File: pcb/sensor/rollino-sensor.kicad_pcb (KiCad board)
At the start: 2 copper layers, 27.5 x 23.2 mm, 14 parts, among them J1 FH12-6S-0.5SH, U1 PMW3610DM-SUDU, U2 TPS7A0518PDBVR

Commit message: Route both PCBs, copper logo, 3D renders of the boards
pcb/gen/route.py has Freerouting route every net (edge and logo keep-outs,
retrying strategies until nothing is left unconnected) and pours GND;
pcb/gen/render_pcbs.sh renders both boards in Blender from KiCad's VRML,
with generated models for the upside-down XIAO and the PMW3610 + lens. The
ROLLINO logo is now bare copper on the back of the band instead of
silkscreen cut by the XIAO's cutout. Connector mounting tabs go to GND;
mounting holes have symbols; the band is 0.5 mm wider for the connectors'
escape routes.

Co-Authored-By: Claude Opus 5.5 <noreply@anthropic.com>
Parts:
- moved U2 0.40 mm to (150.8, 92.1), turned to 180 degrees
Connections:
- net CN renamed /CN
- net CP renamed /CP
- net MOTION renamed /MOTION
- net NCS renamed /NCS
- net NRESET renamed /NRESET
- net SCLK renamed /SCLK
- net SDIO renamed /SDIO
- net VCP renamed /VCP
- net VCSEL+ renamed /VCSEL+
- net VCSEL- renamed /VCSEL-
- J1 pad MP: (no net) -> GND
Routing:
- net +3V3: track 0.00 -> 61.2 mm, vias 0 -> 1
- net GND: track 0.00 -> 59.9 mm, vias 0 -> 1
- net +1V8: track 0.00 -> 48.0 mm, vias 0 -> 1
- net /VCSEL+: track 0.00 -> 46.5 mm, vias 0 -> 1
- net /SDIO: track 0.00 -> 25.5 mm, vias 0 -> 1
- net /SCLK: track 0.00 -> 24.5 mm, vias 0 -> 1
- net /NCS: track 0.00 -> 19.1 mm, vias 0 -> 1
- net /MOTION: track 0.00 -> 13.1 mm, vias 0 -> 1
- net /VCP: track 0.00 -> 5.85 mm, vias 0 -> 1
- net /CP: track 0.00 -> 3.87 mm
- net /CN: track 0.00 -> 2.37 mm
- net /NRESET: track 0.00 -> 2.18 mm
- net /VCSEL-: track 0.00 -> 1.78 mm
- added copper zone on B.Cu, net GND
- added copper zone on F.Cu, net GND
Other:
- board text removed: "ROLLINO SENSOR"

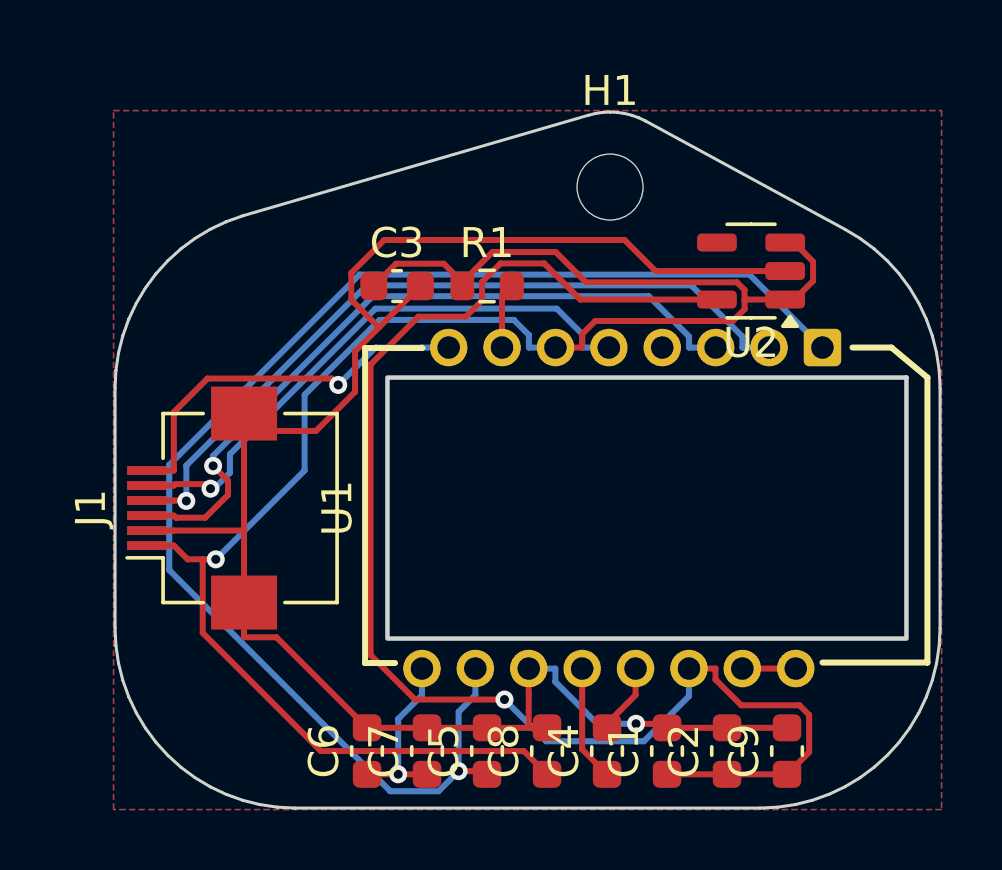
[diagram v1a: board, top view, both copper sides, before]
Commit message: Sensor FPC mouth at the board edge, roomier ribbon channel, clean DRC
The sensor board's FH12 now faces off its up-slope edge, so the ribbon can
be pushed in and latched before the board goes into its pod; the pod has
room for the ribbon's U-turn back over the connector. The ribbon's channel
down through the pod is wider and deeper: part="fpc_check" sweeps a 1.5 mm
thick stand-in along its path and must come out empty, so the free end can
be fed through from either end. Ribbons are 40 mm.

Both boards pass DRC with nothing reported, warnings included: the
regulator moves clear of the sensor's courtyard (its EN tied to VIN by a
locked track route.py keeps), unconnected pins get the schematic's nets,
crowded references go to the fab layer. A small copper ROLLINO logo on the
sensor board's back.

The exploded view is rendered in Blender with KiCad's 3D models of the
boards (case/render_exploded.sh); case/render_previews.sh redoes the
OpenSCAD previews, render_pcbs.sh the layout images and schematic PDFs.

Co-Authored-By: Claude Opus 5.5 <noreply@anthropic.com>
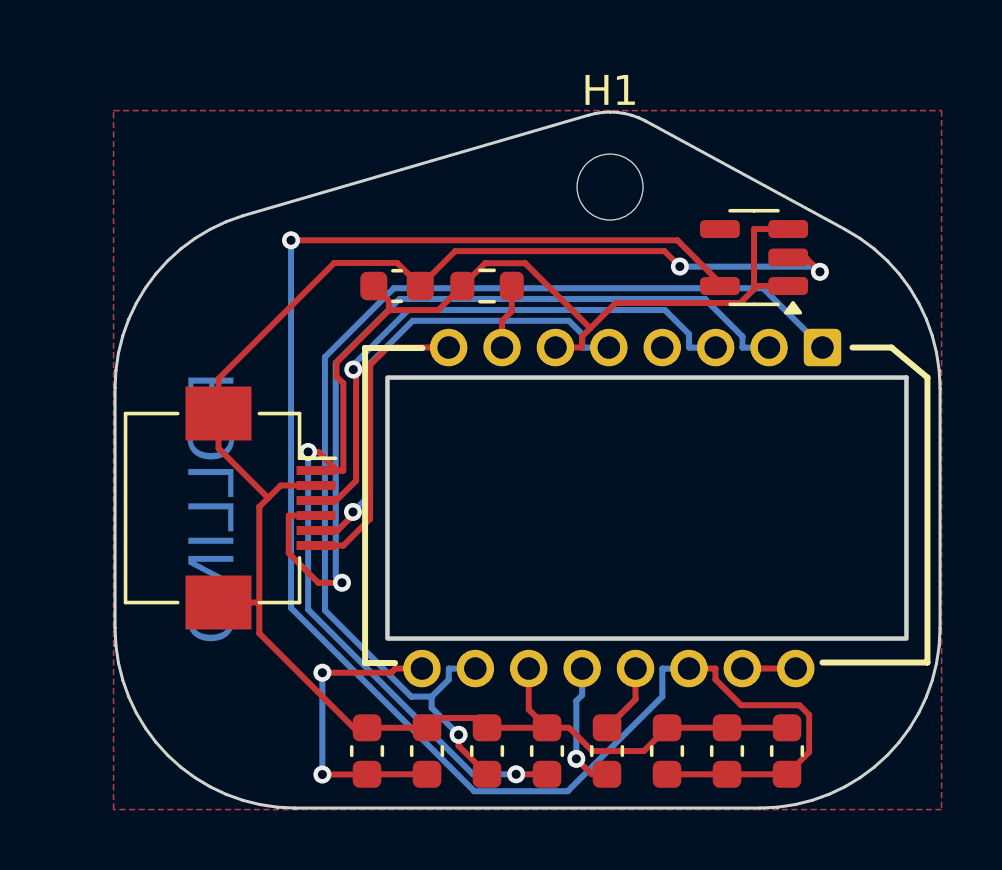
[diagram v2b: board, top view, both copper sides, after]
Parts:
- moved J1 1.95 mm to (134.4, 100.0), turned to -90 degrees
- moved U2 0.46 mm to (150.9, 91.7)
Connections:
- U1 pad 4: (no net) -> unconnected-(U1-NC-Pad4)
- U2 pad 4: (no net) -> unconnected-(U2-NC-Pad4)
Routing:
- net +3V3: track 61.2 -> 45.0 mm, vias 1 -> 2
- net /VCSEL+: track 46.5 -> 37.0 mm
- net +1V8: track 48.0 -> 56.4 mm
- net /SCLK: track 24.5 -> 19.1 mm
- net /VCP: track 5.85 -> 10.3 mm, vias 1 -> 2
- net /NCS: track 19.1 -> 15.9 mm
- net /MOTION: track 13.1 -> 10.2 mm, vias 1 -> 0
- net /SDIO: track 25.5 -> 28.0 mm
- net GND: track 59.9 -> 58.4 mm, vias 1 -> 2
- net /CP: track 3.87 -> 4.33 mm, vias 0 -> 1
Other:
- board text added: "ROLLINO"

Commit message: Shorter base band for a stock 50 mm FFC, parts list, FPC pin order fix
The base board's band now ends at about 110 degrees, with the FPC
connectors lying along it; each ribbon creases flat under its sensor pod
and runs along a channel in the case's underside, held by the cover.
The model solves the crease position from fpc_len = 50 (type B cable).
Connector pins are numbered from the ribbon's path so each signal meets
itself (the flipped sensor connector had reversed them).
Adds parts.md, the parts to order.

Co-Authored-By: Claude Opus 5.5 <noreply@anthropic.com>
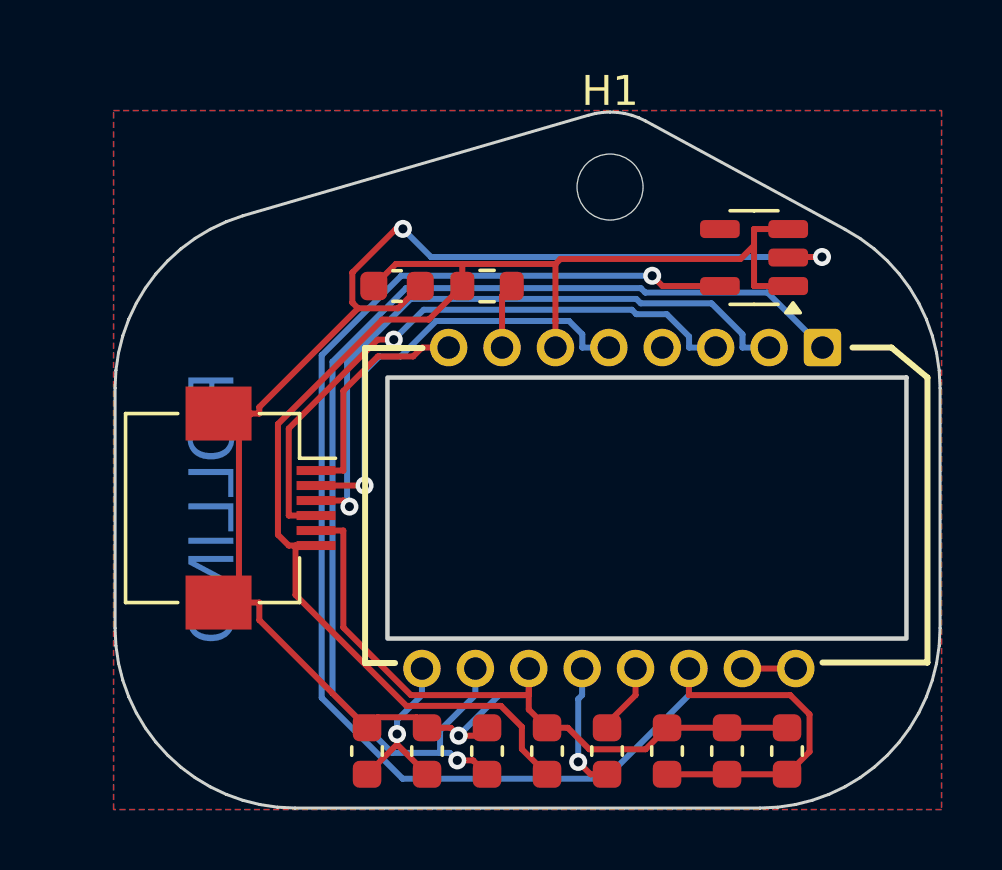
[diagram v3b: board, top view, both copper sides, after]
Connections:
- J1 pad 1: +3V3 -> /MOTION
- J1 pad 2: GND -> /NCS
- J1 pad 3: /SCLK -> /SDIO
- J1 pad 4: /SDIO -> /SCLK
- J1 pad 5: /NCS -> GND
- J1 pad 6: /MOTION -> +3V3
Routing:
- net GND: track 58.4 -> 71.5 mm, vias 2 -> 3
- net /SDIO: track 28.0 -> 21.9 mm
- net /VCP: track 10.3 -> 5.70 mm, vias 2 -> 1
- net +1V8: track 56.4 -> 52.8 mm
- net /MOTION: track 10.2 -> 7.67 mm
- net +3V3: track 45.0 -> 47.0 mm, vias 2 -> 0
- net /VCSEL+: track 37.0 -> 38.8 mm
- net /SCLK: track 19.1 -> 20.4 mm
- net /NCS: track 15.9 -> 14.9 mm

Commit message: Route the base board again, clear the antenna, sensor decoupling by the pins
The base board had come out with nothing routed to its FPC connectors:
Freerouting can't start a track from their pads at this angle. generate.py
now lays a stub out of each pad and route.py has Freerouting join those;
route.py only saves a board that is whole and that KiCad's DRC has nothing
to report on, trying its other strategies otherwise.

Base board: no pour by the XIAO's antenna (the strip between the notch and
the ball's hole), the supply laid across that strip on the back, each
connector's grounds with their own vias to the pours, the pours stitched
together. The bus moves to D4/D5 (the XIAO's only pins that aren't kept
for low frequencies), the right sensor's MOTION to D8, and the buttons are
left, middle, right on D0, D1, D9, so each side's lines stay on its side.

Sensor board: each capacitor by the pin it serves on a short wide track
(PixArt's rule for CP, CN and VCP), the regulator's output capacitor
against it, a ground rail with vias from pin 11, 1.8 V round the lens
cutout on the back, test pads for 1.8 V and GND. Same parts.

Firmware: the new pins, the sensors' angles as the case model has them
now (elevation -22), full transmit power. Case: a hole in the cover under
the XIAO's reset button. The XIAO's 3D model on the base board was a
mirror image.

Co-Authored-By: Claude Opus 5.5 <noreply@anthropic.com>
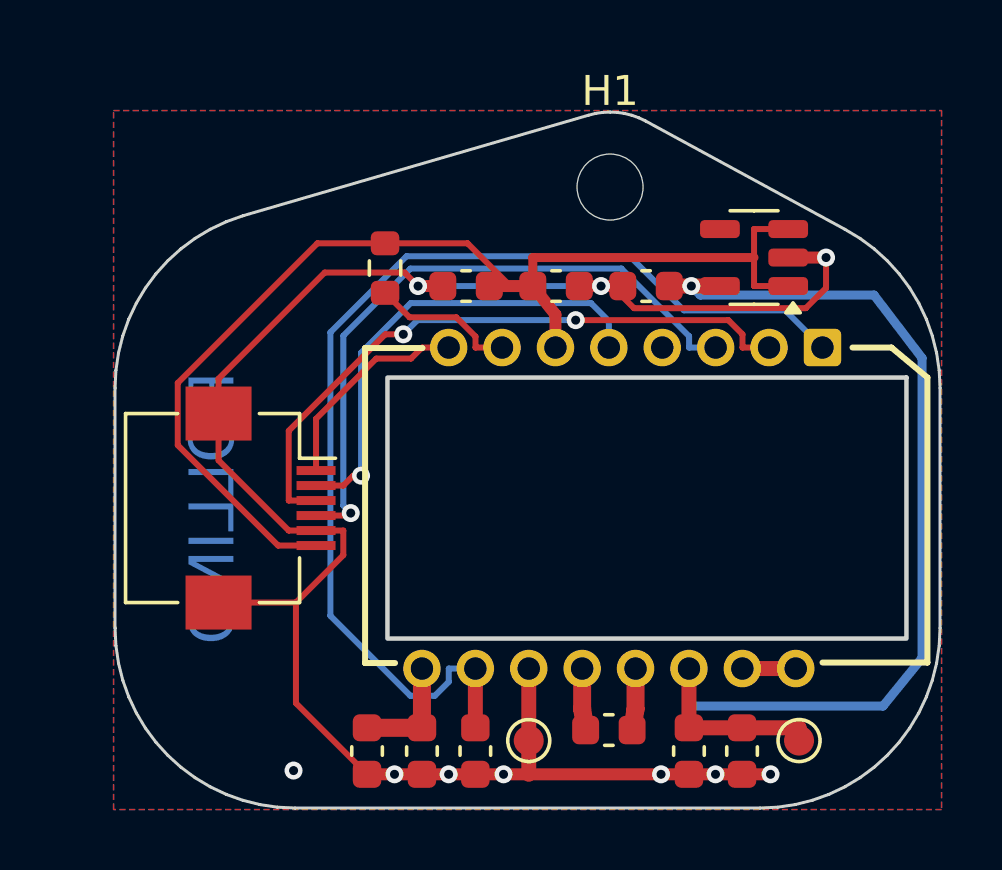
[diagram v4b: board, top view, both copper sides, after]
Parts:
- added TP1: +1V8, TestPoint:TestPoint_Pad_D1.0mm, F.Cu at (152.4, 107.8)
- added TP2: GND, TestPoint:TestPoint_Pad_D1.0mm, F.Cu at (143.4, 107.8)
- moved C9 16.2 mm to (147.3, 92.6), turned to 180 degrees
- moved C8 15.5 mm to (144.3, 92.6), turned to 0 degrees
- moved R1 3.45 mm to (138.6, 92.0), turned to -90 degrees
- moved C1 2.50 mm to (150.5, 108.1), turned to -90 degrees
- moved C3 2.30 mm to (141.3, 92.6), turned to 180 degrees
- moved C2 1.27 mm to (148.7, 108.1), turned to -90 degrees
- moved C4 0.70 mm to (146.1, 107.4), turned to 0 degrees
- moved C5 0.39 mm to (141.6, 108.1), turned to -90 degrees
- moved C7 0.17 mm to (139.8, 108.1), turned to -90 degrees
- turned C6 to -90 degrees
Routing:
- net +1V8: track 52.8 -> 36.4 mm
- net +3V3: track 47.0 -> 37.9 mm
- net GND: track 71.5 -> 63.8 mm, vias 3 -> 10
- net /NRESET: track 2.18 -> 4.87 mm
- net /CP: track 4.30 -> 2.06 mm, vias 1 -> 0
- net /VCSEL+: track 38.8 -> 36.7 mm, vias 1 -> 0
- net /VCP: track 5.70 -> 3.81 mm, vias 1 -> 0
- net /SCLK: track 20.4 -> 21.9 mm
- net /NCS: track 14.9 -> 15.8 mm
- net /MOTION: track 7.67 -> 7.13 mm
- net /SDIO: track 21.9 -> 21.4 mm, vias 1 -> 2
